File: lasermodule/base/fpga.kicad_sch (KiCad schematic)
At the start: 20 parts, among them U12 ICE40UP5K-SG48ITR-FPGA_Lattice, U13 S25FL064LABMFI010, U14 MCP1700x-120xxTT

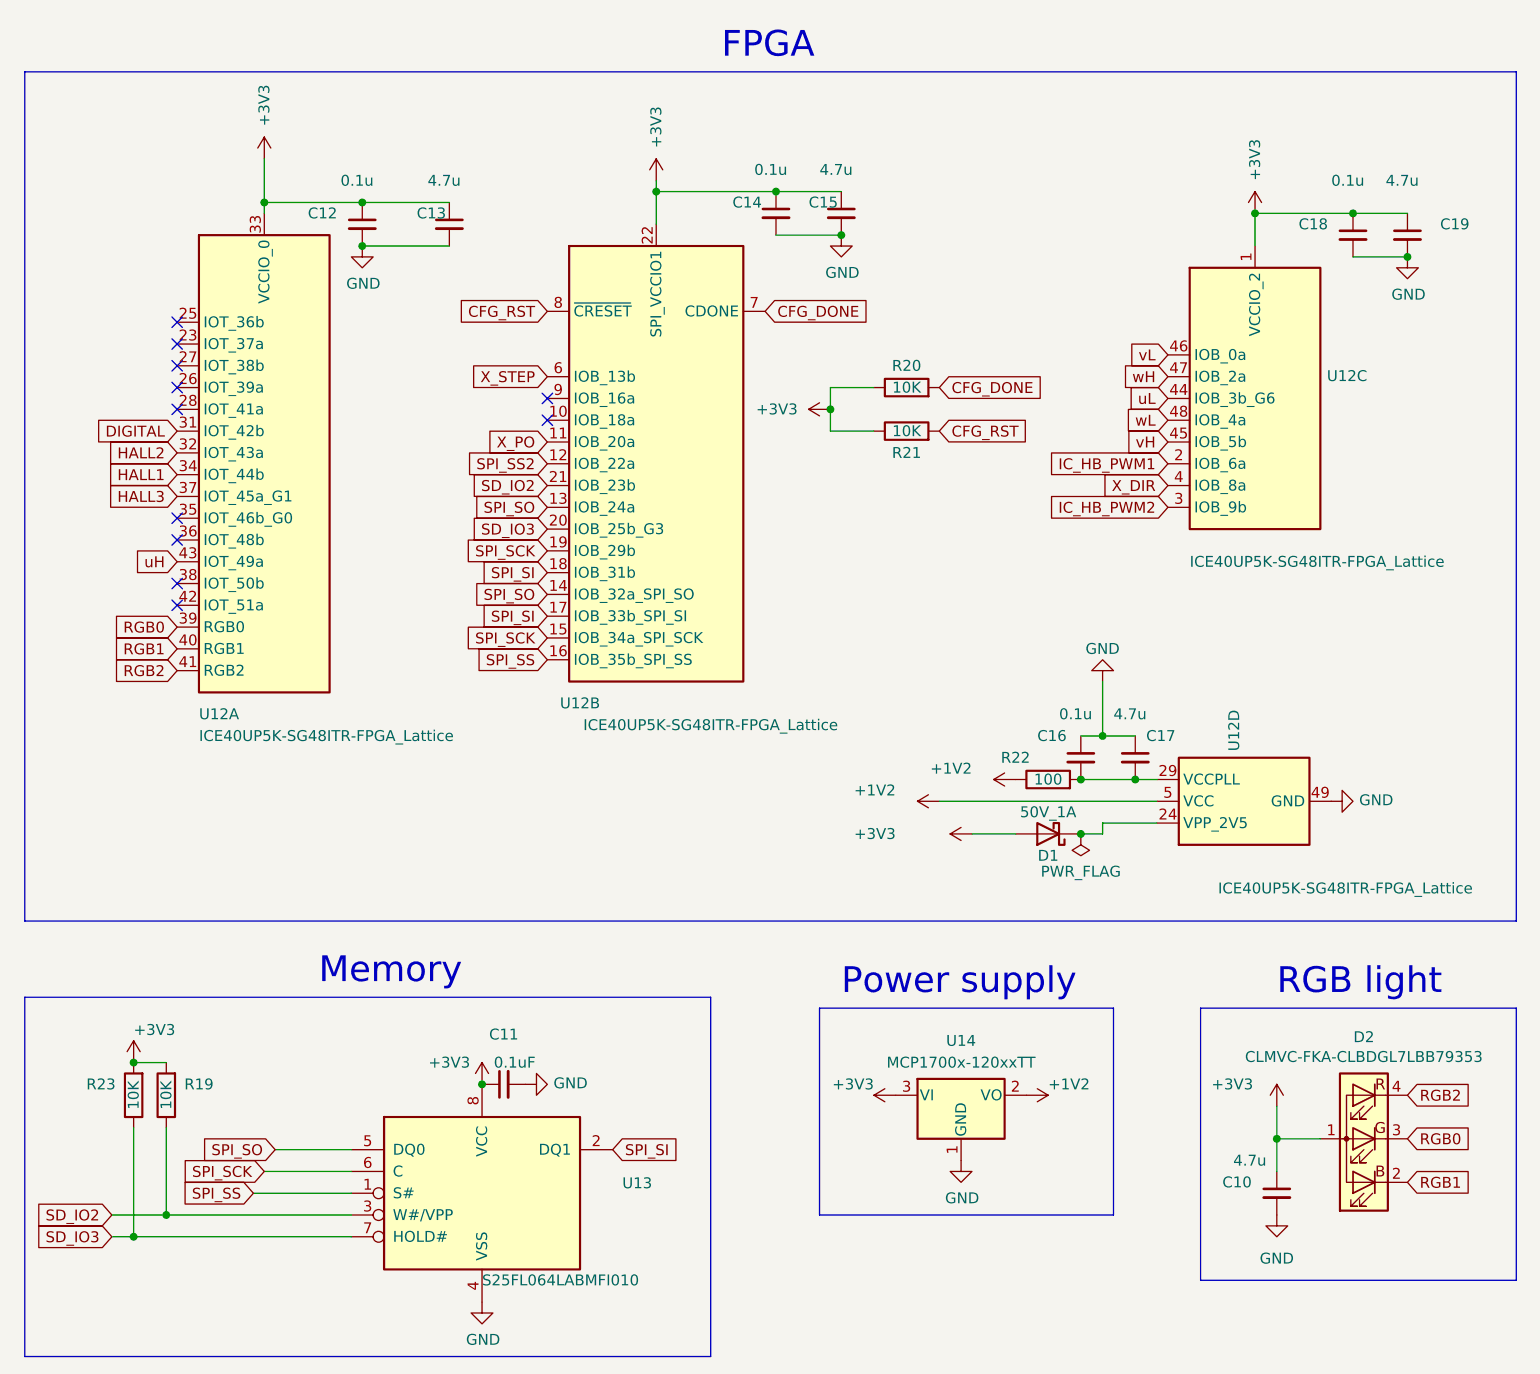
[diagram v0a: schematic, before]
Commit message: improved tracks
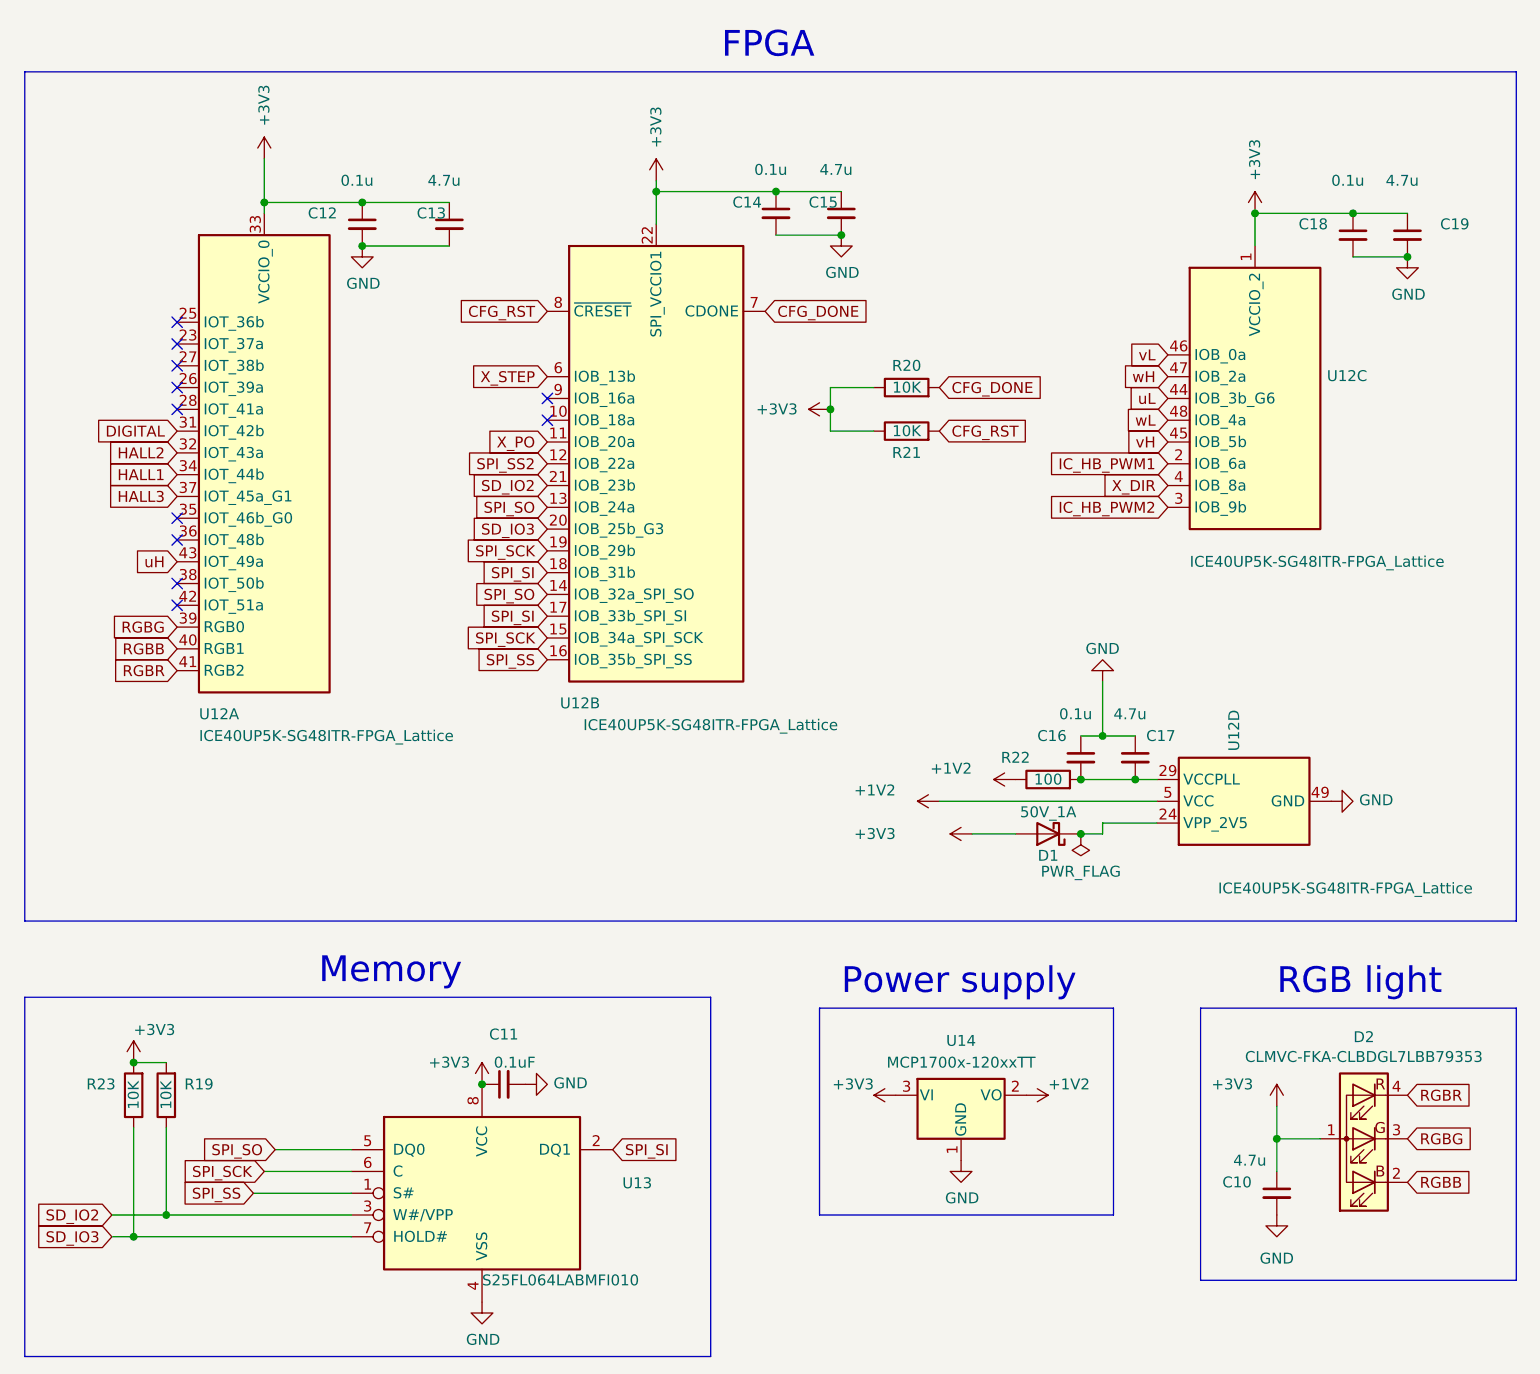
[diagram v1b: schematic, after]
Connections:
- net RGB0 renamed RGBG
- net RGB1 renamed RGBB
- net RGB2 renamed RGBR

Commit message: last save computer battery low
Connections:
- net Z_PO: now reaches U12.26 (IOT_39a)
- net Z_PO: now also U12.35 (IOT_46b_G0)
- net Y_DIR: now reaches U12.27 (IOT_38b)
- net Z_DIR: now reaches U12.28 (IOT_41a)
- net FREE: now reaches U12.36 (IOT_48b)
- net SD_IO2: no longer names the net of R19.1, U13.3 (W#/VPP)
- net SD_IO2: no longer U12.21 (IOB_23b)
- net SD_IO3: no longer names the net of R23.1, U13.7 (HOLD#)
- net SD_IO3: no longer U12.20 (IOB_25b_G3)
- new net Y_PO: U12.21 (IOB_23b)
- new net Y_STEP: U12.20 (IOB_25b_G3)
- no-connect marks 11 -> 6
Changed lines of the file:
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@@
   (junction (at 156.21 62.23) (diameter 0) (color 0 0 0 0)
   )
-  (junction (at 78.74 156.21) (diameter 0) (color 0 0 0 0)
-  )
   (junction (at 185.42 111.76) (diameter 0) (color 0 0 0 0)
   )
@@
   (junction (at 115.57 140.97) (diameter 0) (color 0 0 0 0)
   )
-  (junction (at 74.93 158.75) (diameter 0) (color 0 0 0 0)
-  )
   (junction (at 135.89 36.83) (diameter 0) (color 0 0 0 0)
   )
@@
   (junction (at 101.6 38.1) (diameter 0) (color 0 0 0 0)
   )
-  (no_connect (at 80.01 62.23))
-  (no_connect (at 80.01 74.93))
-  (no_connect (at 80.01 59.69))
-  (no_connect (at 80.01 77.47))
   (no_connect (at 80.01 54.61))
   (no_connect (at 123.19 60.96))
   (no_connect (at 80.01 85.09))
-  (no_connect (at 80.01 57.15))
+  (no_connect (at 80.01 52.07))
   (no_connect (at 80.01 82.55))
-  (no_connect (at 80.01 52.07))
   (no_connect (at 123.19 63.5))
   (wire (pts (xy 111.76 43.18) (xy 101.6 43.18))
@@
     (stroke (width 0) (type default))
   )
-  (wire (pts (xy 72.39 158.75) (xy 74.93 158.75))
-    (stroke (width 0) (type default))
-  )
   (wire (pts (xy 172.72 111.76) (xy 177.8 111.76))
     (stroke (width 0) (type default))
@@
   )
   (wire (pts (xy 90.17 151.13) (xy 100.33 151.13))
-    (stroke (width 0) (type default))
-  )
-  (wire (pts (xy 72.39 156.21) (xy 78.74 156.21))
     (stroke (width 0) (type default))
   )
@@
     (effects (font (size 3 3)) (justify left bottom))
   )
-  (global_label "SD_IO2" (shape input) (at 123.19 71.12 180) (fields_autoplaced)
-    (effects (font (size 1.27 1.27)) (justify right))
-    (property "Intersheetrefs" "${INTERSHEET_REFS}" (at -43.18 21.59 0)
-      (effects (font (size 1.27 1.27)) hide)
+  (global_label "Y_STEP" (shape input) (at 123.19 76.2 180) (fields_autoplaced)
+    (effects (font (size 1.27 1.27)) (justify right))
+    (property "Intersheetrefs" "${INTERSHEET_REFS}" (at 114.2861 76.2 0)
+      (effects (font (size 1.27 1.27)) (justify right) hide)
     )
   )
@@
     )
   )
-  (global_label "SD_IO3" (shape input) (at 123.19 76.2 180) (fields_autoplaced)
+  (global_label "SPI_SI" (shape input) (at 123.19 81.28 180) (fields_autoplaced)
+    (effects (font (size 1.27 1.27)) (justify right))
+    (property "Intersheetrefs" "${INTERSHEET_REFS}" (at 114.9996 81.2006 0)
+      (effects (font (size 1.27 1.27)) (justify right) hide)
+    )
+  )
+  (global_label "SPI_SS" (shape input) (at 123.19 91.44 180) (fields_autoplaced)
+    (effects (font (size 1.27 1.27)) (justify right))
+    (property "Intersheetrefs" "${INTERSHEET_REFS}" (at 114.3948 91.3606 0)
+      (effects (font (size 1.27 1.27)) (justify right) hide)
+    )
+  )
+  (global_label "SPI_SS2" (shape input) (at 123.19 68.58 180) (fields_autoplaced)
+    (effects (font (size 1.27 1.27)) (justify right))
+    (property "Intersheetrefs" "${INTERSHEET_REFS}" (at 113.1853 68.5006 0)
+      (effects (font (size 1.27 1.27)) (justify right) hide)
+    )
+  )
+  (global_label "SPI_SCK" (shape input) (at 90.17 151.13 180) (fields_autoplaced)
+    (effects (font (size 1.27 1.27)) (justify right))
+    (property "Intersheetrefs" "${INTERSHEET_REFS}" (at 80.117 151.13 0)
+      (effects (font (size 1.27 1.27)) (justify right) hide)
+    )
+  )
+  (global_label "X_PO" (shape input) (at 123.19 66.04 180) (fields_autoplaced)
+    (effects (font (size 1.27 1.27)) (justify right))
+    (property "Intersheetrefs" "${INTERSHEET_REFS}" (at -121.92 6.35 0)
+      (effects (font (size 1.27 1.27)) hide)
+    )
+  )
+  (global_label "uL" (shape input) (at 195.58 60.96 180) (fields_autoplaced)
+    (effects (font (size 1.27 1.27)) (justify right))
+    (property "Intersheetrefs" "${INTERSHEET_REFS}" (at 83.82 22.86 0)
+      (effects (font (size 1.27 1.27)) hide)
+    )
+  )
+  (global_label "CFG_RST" (shape input) (at 123.19 50.8 180) (fields_autoplaced)
     (effects (font (size 1.27 1.27)) (justify right))
     (property "Intersheetrefs" "${INTERSHEET_REFS}" (at -43.18 13.97 0)
@@
     )
   )
-  (global_label "SPI_SI" (shape input) (at 123.19 81.28 180) (fields_autoplaced)
-    (effects (font (size 1.27 1.27)) (justify right))
-    (property "Intersheetrefs" "${INTERSHEET_REFS}" (at 114.9996 81.2006 0)
-      (effects (font (size 1.27 1.27)) (justify right) hide)
-    )
-  )
-  (global_label "SPI_SS" (shape input) (at 123.19 91.44 180) (fields_autoplaced)
-    (effects (font (size 1.27 1.27)) (justify right))
-    (property "Intersheetrefs" "${INTERSHEET_REFS}" (at 114.3948 91.3606 0)
-      (effects (font (size 1.27 1.27)) (justify right) hide)
-    )
-  )
-  (global_label "SPI_SS2" (shape input) (at 123.19 68.58 180) (fields_autoplaced)
-    (effects (font (size 1.27 1.27)) (justify right))
-    (property "Intersheetrefs" "${INTERSHEET_REFS}" (at 113.1853 68.5006 0)
-      (effects (font (size 1.27 1.27)) (justify right) hide)
-    )
-  )
-  (global_label "SPI_SCK" (shape input) (at 90.17 151.13 180) (fields_autoplaced)
-    (effects (font (size 1.27 1.27)) (justify right))
-    (property "Intersheetrefs" "${INTERSHEET_REFS}" (at 80.117 151.13 0)
-      (effects (font (size 1.27 1.27)) (justify right) hide)
-    )
-  )
-  (global_label "X_PO" (shape input) (at 123.19 66.04 180) (fields_autoplaced)
-    (effects (font (size 1.27 1.27)) (justify right))
-    (property "Intersheetrefs" "${INTERSHEET_REFS}" (at -121.92 6.35 0)
-      (effects (font (size 1.27 1.27)) hide)
-    )
-  )
-  (global_label "uL" (shape input) (at 195.58 60.96 180) (fields_autoplaced)
-    (effects (font (size 1.27 1.27)) (justify right))
-    (property "Intersheetrefs" "${INTERSHEET_REFS}" (at 83.82 22.86 0)
-      (effects (font (size 1.27 1.27)) hide)
-    )
-  )
-  (global_label "CFG_RST" (shape input) (at 123.19 50.8 180) (fields_autoplaced)
-    (effects (font (size 1.27 1.27)) (justify right))
-    (property "Intersheetrefs" "${INTERSHEET_REFS}" (at -43.18 13.97 0)
-      (effects (font (size 1.27 1.27)) hide)
-    )
-  )
   (global_label "IC_HB_PWM1" (shape input) (at 195.58 68.58 180) (fields_autoplaced)
     (effects (font (size 1.27 1.27)) (justify right))
@@
     )
   )
+  (global_label "Z_PO" (shape input) (at 80.01 59.69 180) (fields_autoplaced)
+    (effects (font (size 1.27 1.27)) (justify right))
+    (property "Intersheetrefs" "${INTERSHEET_REFS}" (at 72.9808 59.69 0)
+      (effects (font (size 1.27 1.27)) (justify right) hide)
+    )
+  )
   (global_label "uH" (shape input) (at 80.01 80.01 180) (fields_autoplaced)
     (effects (font (size 1.27 1.27)) (justify right))
@@
     )
   )
-  (global_label "SD_IO3" (shape input) (at 72.39 158.75 180) (fields_autoplaced)
-    (effects (font (size 1.27 1.27)) (justify right))
-    (property "Intersheetrefs" "${INTERSHEET_REFS}" (at -11.43 39.37 0)
-      (effects (font (size 1.27 1.27)) hide)
-    )
-  )
   (global_label "SPI_SO" (shape input) (at 123.19 83.82 180) (fields_autoplaced)
     (effects (font (size 1.27 1.27)) (justify right))
@@
     )
   )
+  (global_label "Z_PO" (shape input) (at 80.01 74.93 180) (fields_autoplaced)
+    (effects (font (size 1.27 1.27)) (justify right))
+    (property "Intersheetrefs" "${INTERSHEET_REFS}" (at 72.9808 74.93 0)
+      (effects (font (size 1.27 1.27)) (justify right) hide)
+    )
+  )
+  (global_label "Y_PO" (shape input) (at 123.19 71.12 180) (fields_autoplaced)
+    (effects (font (size 1.27 1.27)) (justify right))
+    (property "Intersheetrefs" "${INTERSHEET_REFS}" (at 116.2817 71.12 0)
+      (effects (font (size 1.27 1.27)) (justify right) hide)
+    )
+  )
   (global_label "RGBG" (shape input) (at 80.01 87.63 180) (fields_autoplaced)
     (effects (font (size 1.27 1.27)) (justify right))
@@
     (effects (font (size 1.27 1.27)) (justify right))
     (property "Intersheetrefs" "${INTERSHEET_REFS}" (at 82.5965 148.59 0)
+      (effects (font (size 1.27 1.27)) (justify right) hide)
+    )
+  )
+  (global_label "Z_DIR" (shape input) (at 80.01 62.23 180) (fields_autoplaced)
+    (effects (font (size 1.27 1.27)) (justify right))
+    (property "Intersheetrefs" "${INTERSHEET_REFS}" (at 72.4365 62.23 0)
+      (effects (font (size 1.27 1.27)) (justify right) hide)
+    )
+  )
+  (global_label "FREE" (shape input) (at 80.01 77.47 180) (fields_autoplaced)
+    (effects (font (size 1.27 1.27)) (justify right))
+    (property "Intersheetrefs" "${INTERSHEET_REFS}" (at 73.1018 77.47 0)
       (effects (font (size 1.27 1.27)) (justify right) hide)
     )
@@
     )
   )
-  (global_label "SD_IO2" (shape input) (at 72.39 156.21 180) (fields_autoplaced)
-    (effects (font (size 1.27 1.27)) (justify right))
-    (property "Intersheetrefs" "${INTERSHEET_REFS}" (at -11.43 39.37 0)
-      (effects (font (size 1.27 1.27)) hide)
-    )
-  )
   (global_label "vH" (shape input) (at 195.58 66.04 180) (fields_autoplaced)
     (effects (font (size 1.27 1.27)) (justify right))
@@
     )
   )
+  (global_label "Y_DIR" (shape input) (at 80.01 57.15 180) (fields_autoplaced)
+    (effects (font (size 1.27 1.27)) (justify right))
+    (property "Intersheetrefs" "${INTERSHEET_REFS}" (at 72.5574 57.15 0)
+      (effects (font (size 1.27 1.27)) (justify right) hide)
+    )
+  )
